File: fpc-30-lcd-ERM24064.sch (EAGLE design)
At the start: 21 parts

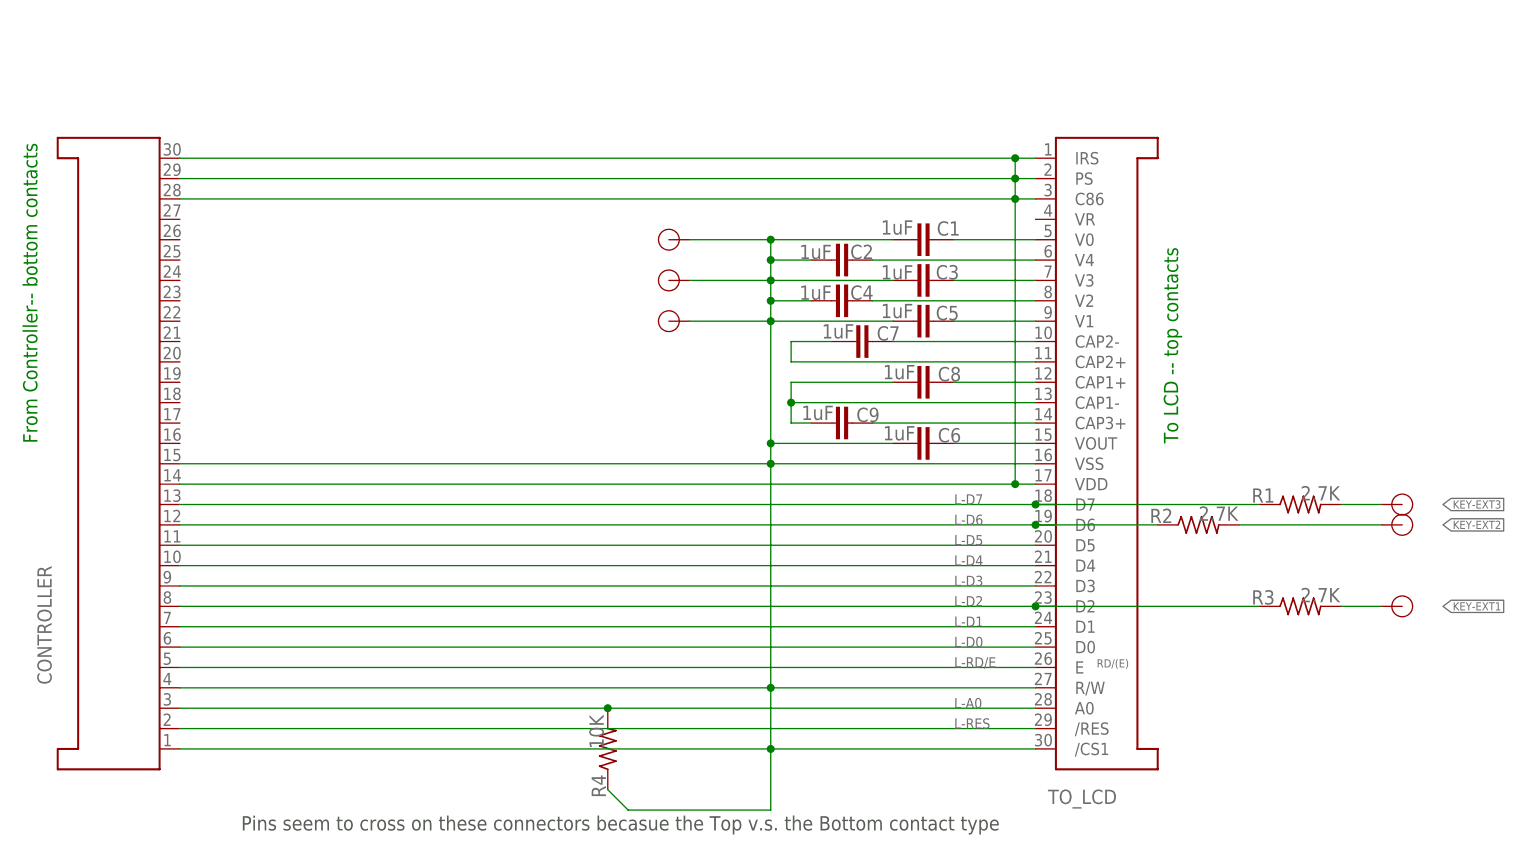
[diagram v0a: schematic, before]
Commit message: added pictures and docs added firmware binary added old JR9303 wiring and pin-out doc added lcd display adapter patch boards for different displays
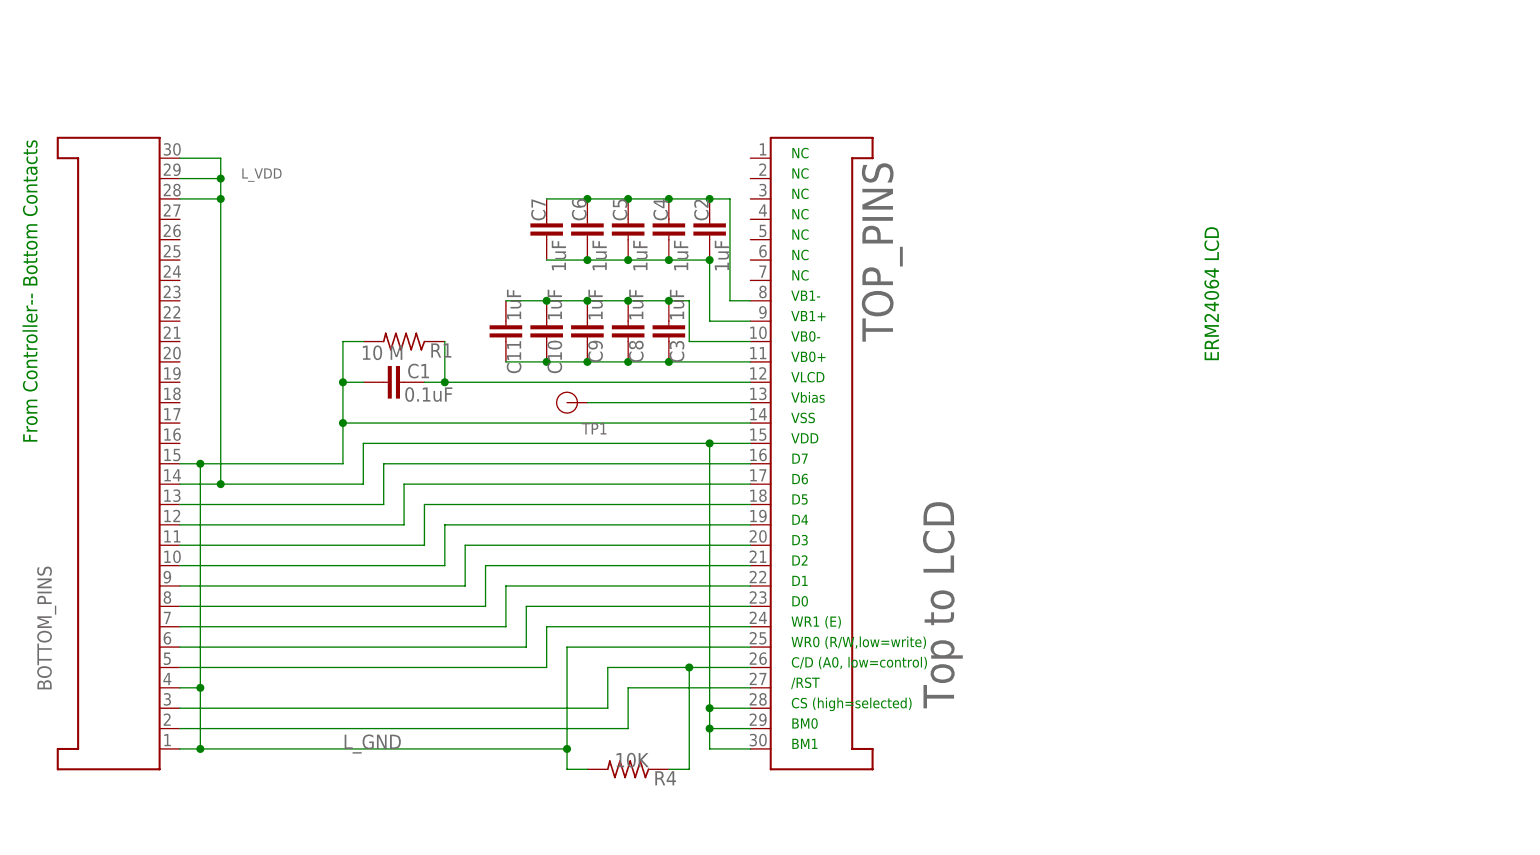
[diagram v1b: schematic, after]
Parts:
- removed EXT1, EXT2, EXT3, K_EXT4, K_EXT5, K_EXT6: TP-1, XP9300:TP-1
- removed R2, R3: 2.7K, rcl:R-US_R0603
- removed TO_LCD: FPC30 - Bottom-pins, XP9300:FPC_30_ERC12864-2
- added C10, C11: 1uF, rcl:C-EUC0603K
- added TOP_PINS: Top to LCD, XP9300:FPC_30-PINS
- added TP1: TP-1, XP9300:TP-1
- BOTTOM_PINS: value FPC30-Top_pins -> FPC30-bottom_pins
- C1: value 1uF -> 0.1uF; device rcl:C-EUC0805 -> rcl:C-EUC0603K
- C2, C3, C4, C5, C6, C7, C8, C9: device rcl:C-EUC0805 -> rcl:C-EUC0603K
- R1: value 2.7K -> 10 M
- renumbered CONTROLLER to BOTTOM_PINS
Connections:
- removed net KEY-EXT1: EXT1.P$1, R3.2
- removed net KEY-EXT2: EXT2.P$1, R2.2
- removed net KEY-EXT3: EXT3.P$1, R1.2
- removed net L-D2: BOTTOM_PINS.P$8, R3.1, TO_LCD.D2
- removed net L-D7: BOTTOM_PINS.P$13, R1.1, TO_LCD.D7
- removed net N$10: C7.2, TO_LCD.CAP2+
- removed net N$11: C8.2, C9.2, TO_LCD.CAP1-
- removed net N$12: C8.1, TO_LCD.CAP1+
- removed net N$14: C9.1, TO_LCD.CAP3+
- removed net N$15: C6.1, TO_LCD.VOUT
- removed net N$3: C1.1, TO_LCD.V0
- removed net N$9: C7.1, TO_LCD.CAP2-
- new net L_D7: BOTTOM_PINS.P$13, TOP_PINS.P$16
- new net N$1: C1.1, R1.1, TOP_PINS.P$12
- new net N$13: BOTTOM_PINS.P$8, TOP_PINS.P$21
- new net N$2: TOP_PINS.P$13, TP1.P$1
- net L-A0: now also R4.1, TOP_PINS.P$26; no longer R4.2, TO_LCD.A0
- net L-D0: now also TOP_PINS.P$23; no longer TO_LCD.D0
- net L-D1: now also TOP_PINS.P$22; no longer TO_LCD.D1
- net L-D3: now also TOP_PINS.P$20; no longer TO_LCD.D3
- net L-D4: now also TOP_PINS.P$19; no longer TO_LCD.D4
- net L-D5: now also TOP_PINS.P$18; no longer TO_LCD.D5
- net L-D6: now also TOP_PINS.P$17; no longer R2.1, TO_LCD.D6
- net L-RD/E: now also TOP_PINS.P$24; no longer TO_LCD.E
- net L-RES: now also TOP_PINS.P$27; no longer TO_LCD./RES
- net L_GND: now also R1.2, R4.2, TOP_PINS.P$14, TOP_PINS.P$25; no longer C2.2, C3.2, C4.2, C5.2, C6.2, K_EXT4.P$1, K_EXT5.P$1, K_EXT6.P$1, R4.1, TO_LCD./CS1, TO_LCD.R/W, TO_LCD.VSS
- net L_VDD: now also TOP_PINS.P$15, TOP_PINS.P$28, TOP_PINS.P$29, TOP_PINS.P$30; no longer TO_LCD.C86, TO_LCD.IRS, TO_LCD.PS, TO_LCD.VDD
- net N$4: now also C4.1, C5.1, C6.1, C7.1, TOP_PINS.P$8; no longer TO_LCD.V4
- net N$5: now also C10.2, C11.2, C3.2, C8.2, C9.2, TOP_PINS.P$10; no longer C3.1, TO_LCD.V3
- net N$6: now also C2.2, C4.2, C5.2, C6.2, C7.2, TOP_PINS.P$9; no longer C4.1, TO_LCD.V2
- net N$7: now also C10.1, C11.1, C3.1, C8.1, C9.1, TOP_PINS.P$11; no longer C5.1, TO_LCD.V1
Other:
- note added: "/RST"
- note added: "BM0"
- note added: "BM1"
- note added: "C/D (A0, low=control)"
- note added: "CS (high=selected)"
- note added: "D0"
- note added: "D1"
- note added: "D2"
- note added: "D3"
- note added: "D4"
- note added: "D5"
- note added: "D6"
- note added: "D7"
- note added: "ERM24064 LCD"
- note added: "From Controller-- Bottom Contacts"
- note added: "NC"
- note added: "VB0+"
- note added: "VB0-"
- note added: "VB1+"
- note added: "VB1-"
- note added: "VDD"
- note added: "VLCD"
- note added: "VSS"
- note added: "Vbias"
- note added: "WR0 (R/W,low=write)"
- note added: "WR1 (E)"
- note removed: "From Controller-- bottom contacts"
- note removed: "Pins seem to cross on these connectors becasue the Top v.s. the Bottom contact type"
- note removed: "RD/(E)"
- note removed: "To LCD -- top contacts"
- moved on the sheet: C1, C2, C3, C4, C5, C6, C7, C8, C9, R1, R4
